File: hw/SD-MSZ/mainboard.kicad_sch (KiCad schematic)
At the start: 56 parts, among them J1 Conn_02x04 HDR, J14 Conn_01x02 HDR, J2 Conn_01x02, J24 Conn_01x02 HDR, J3 Conn_02x05_Odd_Even, Q1 2N3904, Q2 2N3904, Q3 2N3904, Q4 2N3904, Q5 2N3904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

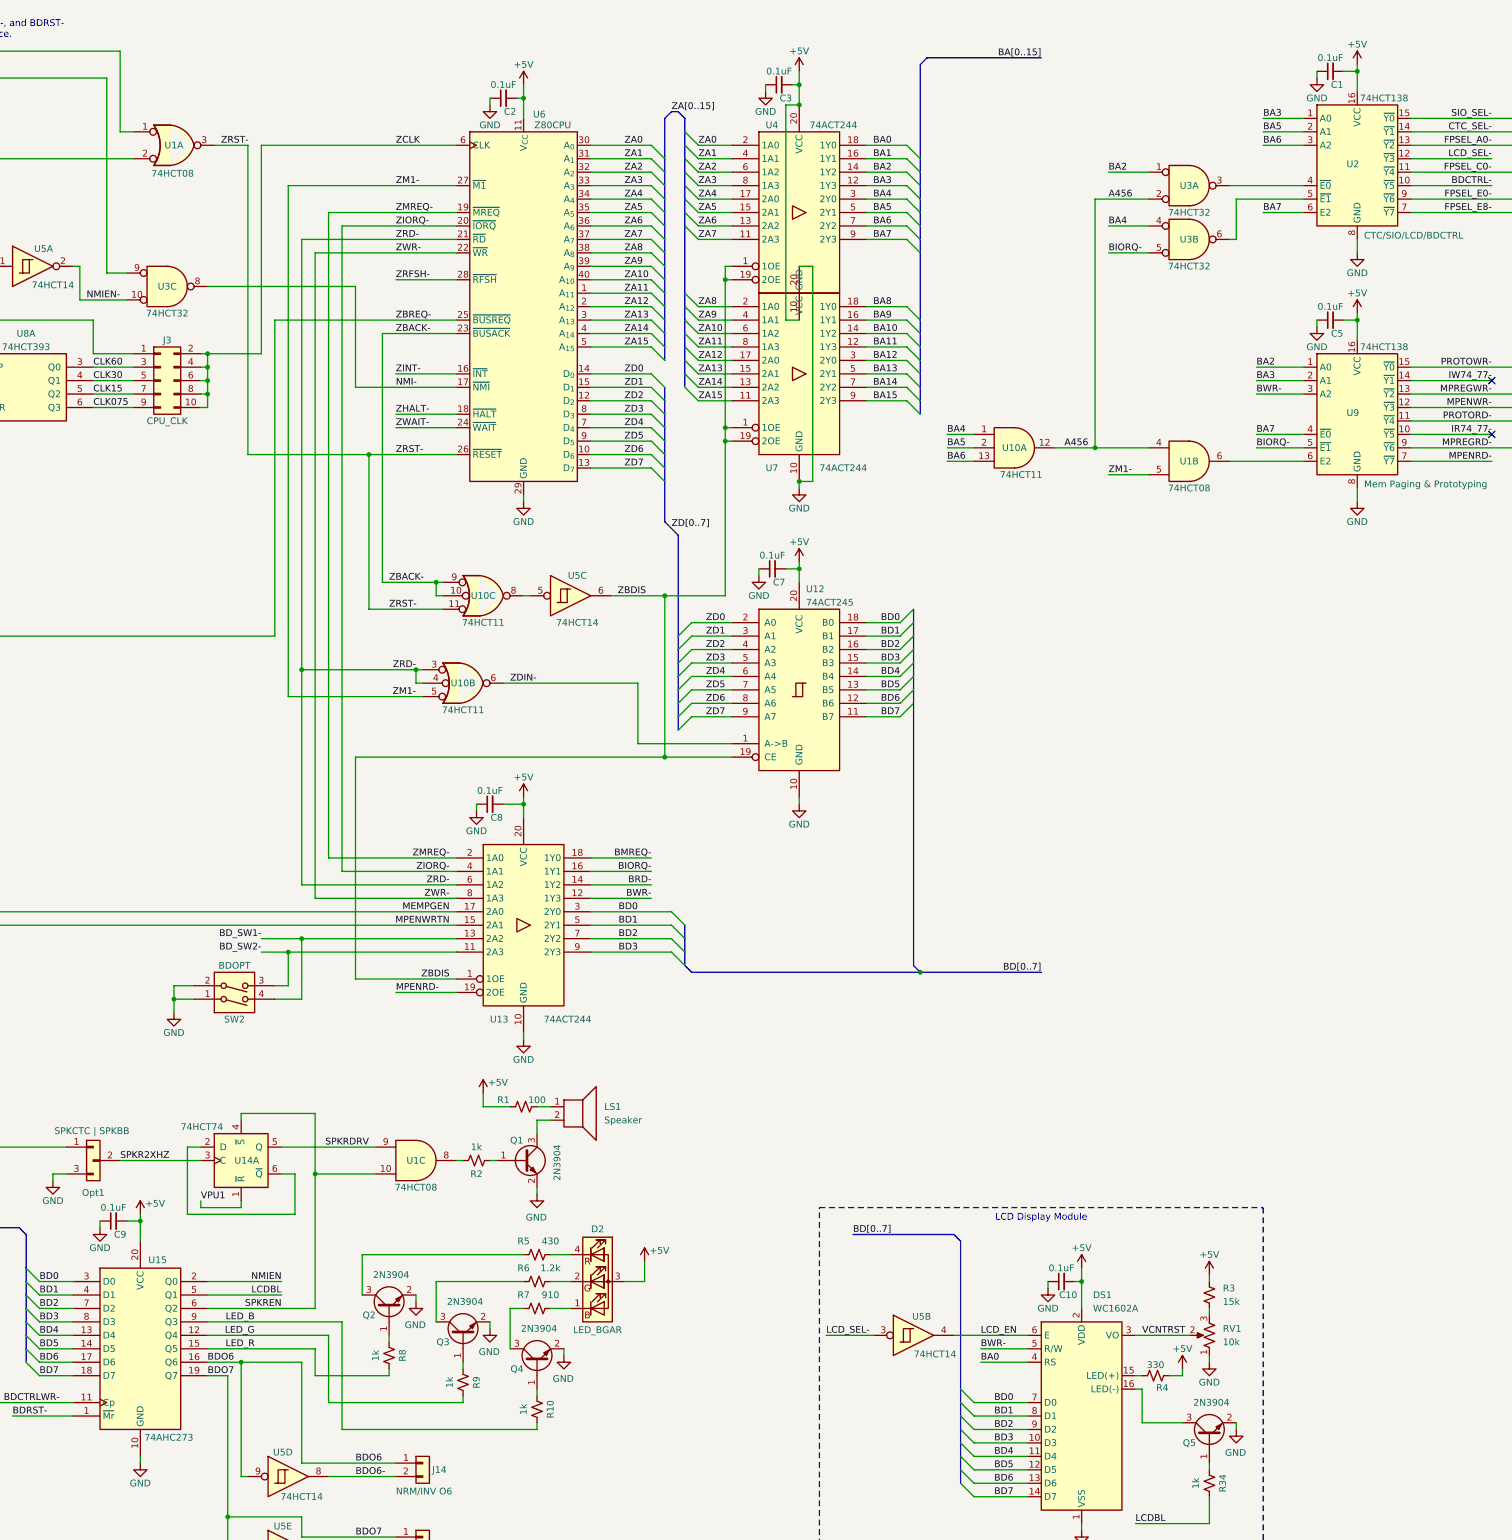
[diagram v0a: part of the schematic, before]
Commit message: Update gitignore to skip KiCad lock and backup files.
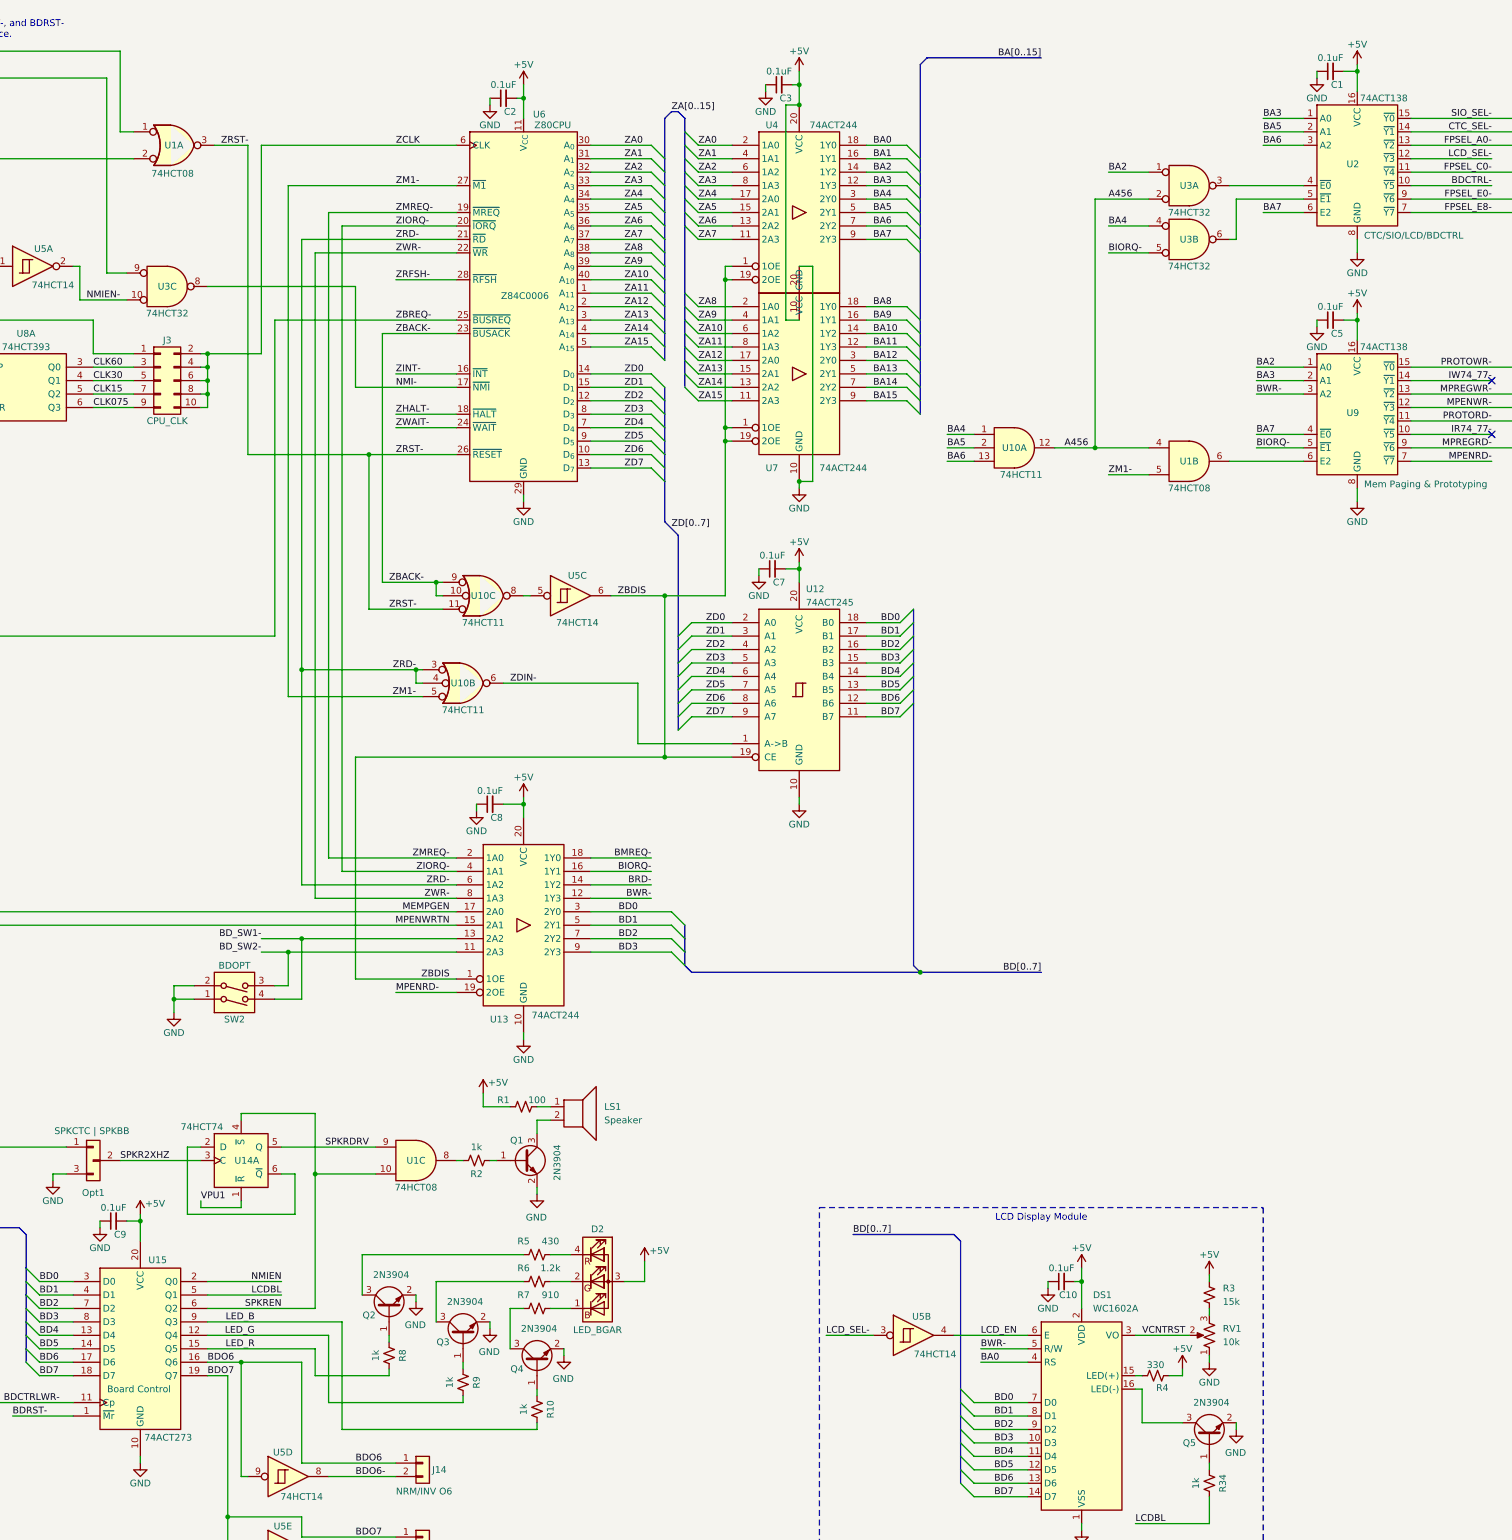
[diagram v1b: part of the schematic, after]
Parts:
- U15: value 74AHC273 -> 74ACT273; Function (none) -> Board Control
- U2, U9: value 74HCT138 -> 74ACT138
- U6: Part (none) -> Z84C0006
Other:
- company: Silky Design -> SilkyDESIGN
- title: Main Board - Z80, Memory, I/O, Exp -> Z80, Clk, Rst, Bus, Decode, Indicators
